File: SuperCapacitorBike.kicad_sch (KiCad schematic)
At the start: 13 parts, among them J1 Screw_Terminal_01x04, K1 AWHSH105D00G, K2 AWHSH105D00G, Q1 IRF540N, U1 LM741, U2 MCP4161

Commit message: Improved filtering & Relay logic
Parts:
- removed C2: 0.1uF, symbol Device:C_Polarized_Small
- added C3: 0.1uF, symbol Device:C_Polarized_Small
- added R5, R6: 50Ω, symbol Device:R_US
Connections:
- net 5V: now also C3.1
- net DC2+: now also K1.1; no longer K1.2
- net DC2-: now also K2.1; no longer K2.2
- net GND: now also C3.2, R5.2, R6.2; no longer K1.1, K2.1
- new net: K1.2, R5.1
- new net: K2.2, R6.1

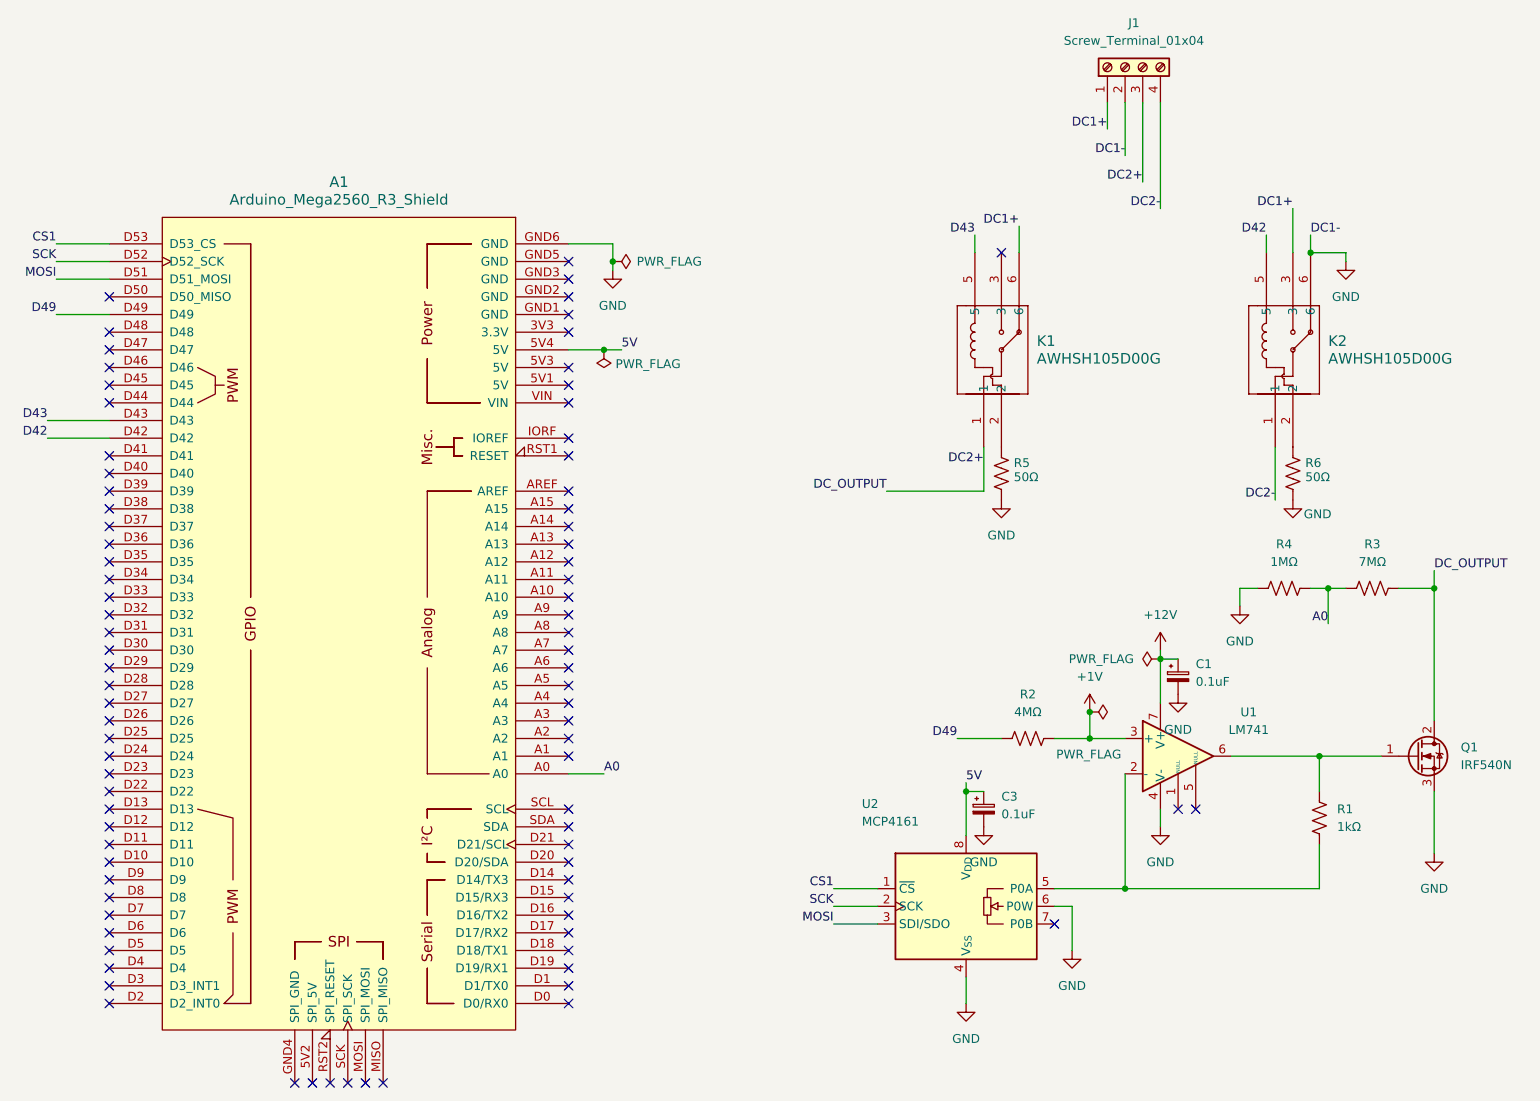
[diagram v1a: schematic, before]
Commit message: Complete redesign of the schematic
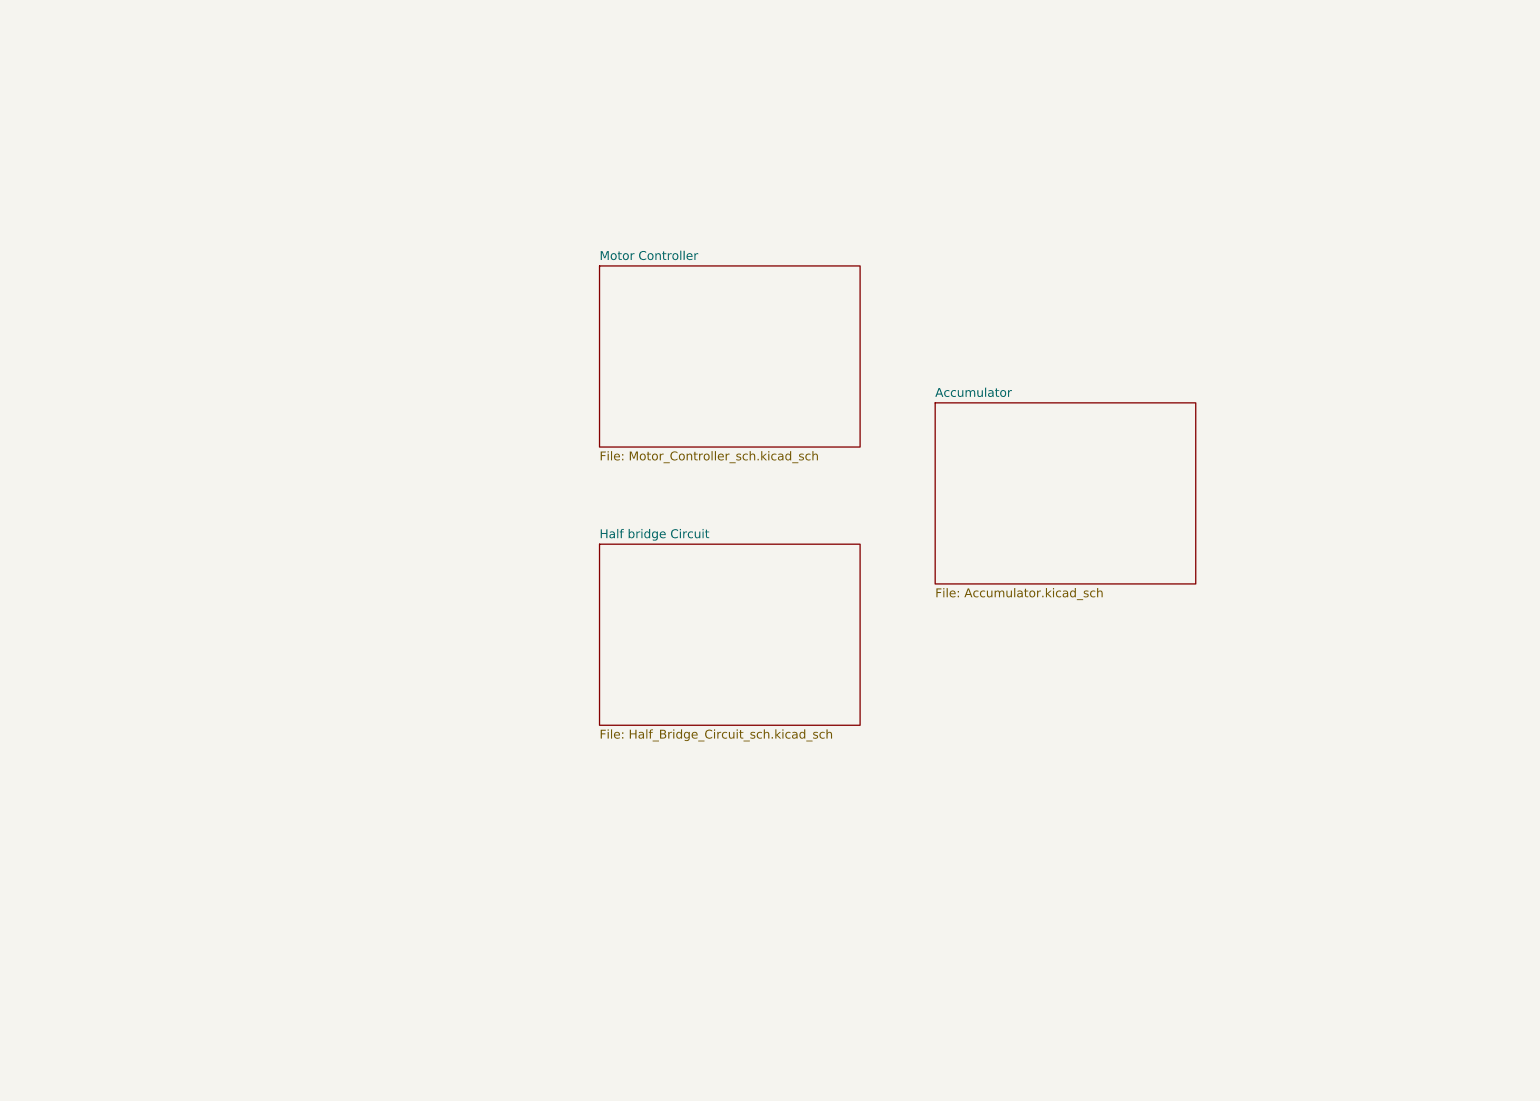
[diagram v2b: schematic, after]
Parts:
- removed A1: Arduino_Mega2560_R3_Shield, PCM_arduino-library:Arduino_Mega2560_R3_Shield, symbol arduino-library:Arduino_Mega2560_R3_Shield
- removed C1, C3: 0.1uF, symbol Device:C_Polarized_Small
- removed J1: Screw_Terminal_01x04, symbol Connector:Screw_Terminal_01x04
- removed K1, K2: AWHSH105D00G, AWHSH1xxD00G_AMP, symbol 2024-06-29_06-24-28:AWHSH105D00G
- removed Q1: IRF540N, Package_TO_SOT_THT:TO-220-3_Vertical, symbol Transistor_FET:IRF540N
- removed R1: 1kΩ, symbol Device:R_US
- removed R2: 4MΩ, symbol Device:R_US
- removed R3: 7MΩ, symbol Device:R_US
- removed R4: 1MΩ, symbol Device:R_US
- removed R5, R6: 50Ω, symbol Device:R_US
- removed U1: LM741, symbol Amplifier_Operational:LM741
- removed U2: MCP4161, Package_DIP:DIP-8_W7.62mm, symbol Potentiometer_Digital:MCP4161-xxxx-P
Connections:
- no-connect marks 86 -> 0
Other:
- added sheet Accumulator (Accumulator.kicad_sch)
- added sheet Half bridge Circuit (Half_Bridge_Circuit_sch.kicad_sch)
- added sheet Motor Controller (Motor_Controller_sch.kicad_sch)
